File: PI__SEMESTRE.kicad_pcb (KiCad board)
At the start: 2 copper layers, 32 parts, among them IC1 LMV358IDR, J1 CX90B-16P1, U1 AMS1117, U11 ESP32-S3-WROOM-1, U14 BME688, U9 GUVA-S12SD

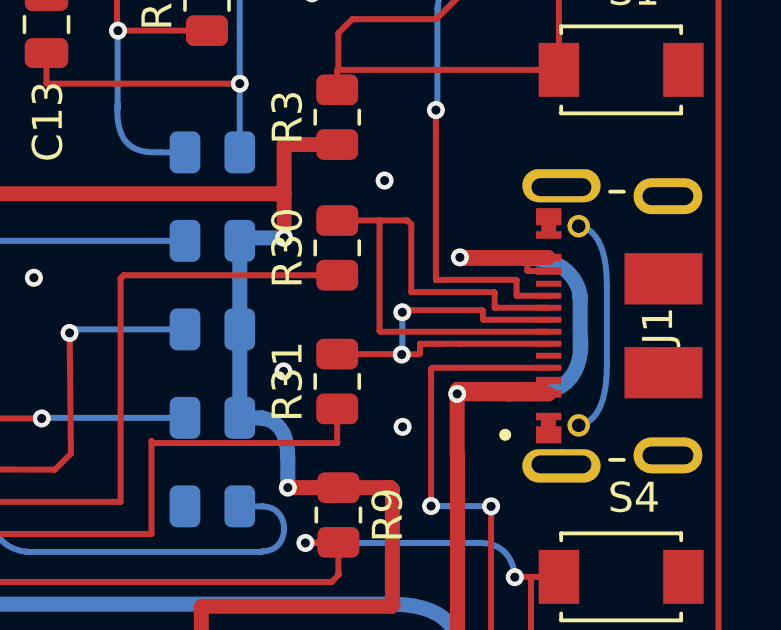
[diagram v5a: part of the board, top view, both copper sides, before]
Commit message: empece atrabajar las pistas rojas de la pcb
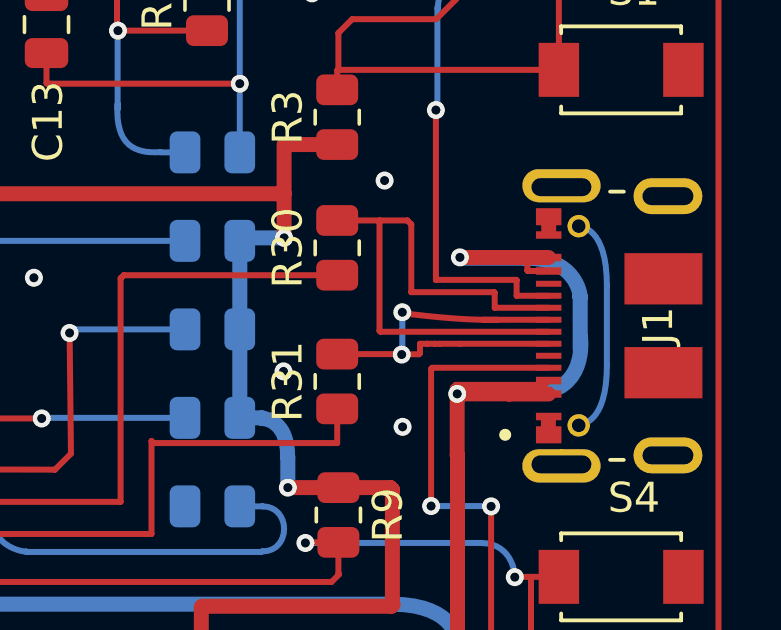
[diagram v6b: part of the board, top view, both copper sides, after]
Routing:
- net D+: track 14.1 -> 11.3 mm
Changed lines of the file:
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@@
 	(gr_curve
 		(pts
+			(xy 121.58 77.96) (xy 120.13 77.99) (xy 118.57 77.74) (xy 118.42 77.75)
+		)
+		(stroke
+			(width 0.2)
+			(type default)
+		)
+		(layer "F.Cu")
+		(net "D+")
+	)
+	(gr_curve
+		(pts
 			(xy 71.7 69.71) (xy 71.72 66.97) (xy 73.91 66.95) (xy 74.236277 66.935356)
 		)
@@
 	)
 	(segment
+		(start 83.05 72.98)
+		(end 83.05 75.82)
+		(width 0.2)
+		(layer "F.Cu")
+		(net "GPIO2")
+	)
+	(segment
+		(start 73.06 72.98)
+		(end 83.05 72.98)
+		(width 0.2)
+		(layer "F.Cu")
+		(net "GPIO2")
+	)
+	(segment
+		(start 72.96 72.88)
+		(end 73.06 72.98)
+		(width 0.2)
+		(layer "F.Cu")
+		(net "GPIO2")
+	)
+	(segment
+		(start 83.05 75.82)
+		(end 83.055 75.825)
+		(width 0.2)
+		(layer "F.Cu")
+		(net "GPIO2")
+	)
+	(segment
+		(start 83.055 75.825)
+		(end 83.14 75.91)
+		(width 0.2)
+		(layer "F.Cu")
+		(net "GPIO2")
+	)
+	(segment
+		(start 98.11 87.84)
+		(end 96.12 87.84)
+		(width 0.2)
+		(layer "F.Cu")
+		(net "GPIO2")
+	)
+	(segment
+		(start 98.11 89.07)
+		(end 98.11 87.84)
+		(width 0.2)
+		(layer "F.Cu")
+		(net "GPIO2")
+	)
+	(segment
+		(start 72.96 69.66)
+		(end 72.96 72.88)
+		(width 0.2)
+		(layer "F.Cu")
+		(net "GPIO2")
+	)
+	(via
+		(at 83.055 75.825)
+		(size 0.6)
+		(drill 0.3)
+		(layers "F.Cu" "B.Cu")
+		(net "GPIO2")
+	)
+	(via
+		(at 96.12 87.84)
+		(size 0.6)
+		(drill 0.3)
+		(layers "F.Cu" "B.Cu")
+		(net "GPIO2")
+	)
+	(segment
+		(start 83.055 75.825)
+		(end 83.01 75.87)
+		(width 0.2)
+		(layer "B.Cu")
+		(net "GPIO2")
+	)
+	(segment
+		(start 84.58 94.82)
+		(end 94.85 94.82)
+		(width 0.2)
+		(layer "B.Cu")
+		(net "GPIO2")
+	)
+	(segment
+		(start 83.01 75.87)
+		(end 83.01 93.25)
+		(width 0.2)
+		(layer "B.Cu")
+		(net "GPIO2")
+	)
+	(segment
+		(start 96.08 87.88)
+		(end 96.12 87.84)
+		(width 0.2)
+		(layer "B.Cu")
+		(net "GPIO2")
+	)
+	(segment
+		(start 96.08 93.53)
+		(end 96.08 87.88)
+		(width 0.2)
+		(layer "B.Cu")
+		(net "GPIO2")
+	)
+	(segment
 		(start 115.2 85.38)
 		(end 116.28 85.38)
@@
 	)
 	(segment
-		(start 118.686029 77.64)
-		(end 121.07 77.64)
-		(width 0.2)
-		(layer "F.Cu")
-		(net "D+")
-	)
-	(segment
-		(start 121.1 77.67)
-		(end 121.1 77.94)
-		(width 0.2)
-		(layer "F.Cu")
-		(net "D+")
-	)
-	(segment
 		(start 119 79.08)
 		(end 118.97 79.11)
@@
 	)
 	(segment
-		(start 121.07 77.64)
-		(end 121.1 77.67)
-		(width 0.2)
-		(layer "F.Cu")
-		(net "D+")
-	)
-	(segment
 		(start 119.504719 78.76)
 		(end 119.662915 78.76)
@@
 	)
 	(segment
-		(start 121.1 77.94)
-		(end 121.12 77.96)
-		(width 0.2)
-		(layer "F.Cu")
-		(net "D+")
-	)
-	(segment
 		(start 118.4 79.11)
 		(end 118.39 79.12)
@@
 	)
 	(segment
-		(start 118.616029 77.71)
-		(end 118.686029 77.64)
-		(width 0.2)
-		(layer "F.Cu")
-		(net "D+")
-	)
-	(segment
 		(start 118.41 77.71)
 		(end 118.616029 77.71)
@@
 		(net "Net-(J1-MID_PLATE-PadMID1)")
 	)
-	(segment
-		(start 83.05 72.98)
-		(end 83.05 75.82)
-		(width 0.2)
-		(layer "F.Cu")
-		(net "GPIO2")
-	)
-	(segment
-		(start 73.06 72.98)
-		(end 83.05 72.98)
-		(width 0.2)
-		(layer "F.Cu")
-		(net "GPIO2")
-	)
-	(segment
-		(start 72.96 72.88)
-		(end 73.06 72.98)
-		(width 0.2)
-		(layer "F.Cu")
-		(net "GPIO2")
-	)
-	(segment
-		(start 83.05 75.82)
-		(end 83.055 75.825)
-		(width 0.2)
-		(layer "F.Cu")
-		(net "GPIO2")
-	)
-	(segment
-		(start 83.055 75.825)
-		(end 83.14 75.91)
-		(width 0.2)
-		(layer "F.Cu")
-		(net "GPIO2")
-	)
-	(segment
-		(start 98.11 87.84)
-		(end 96.12 87.84)
-		(width 0.2)
-		(layer "F.Cu")
-		(net "GPIO2")
-	)
-	(segment
-		(start 98.11 89.07)
-		(end 98.11 87.84)
-		(width 0.2)
-		(layer "F.Cu")
-		(net "GPIO2")
-	)
-	(segment
-		(start 72.96 69.66)
-		(end 72.96 72.88)
-		(width 0.2)
-		(layer "F.Cu")
-		(net "GPIO2")
-	)
-	(via
-		(at 83.055 75.825)
-		(size 0.6)
-		(drill 0.3)
-		(layers "F.Cu" "B.Cu")
-		(net "GPIO2")
-	)
-	(via
-		(at 96.12 87.84)
-		(size 0.6)
-		(drill 0.3)
-		(layers "F.Cu" "B.Cu")
-		(net "GPIO2")
-	)
-	(segment
-		(start 83.055 75.825)
-		(end 83.01 75.87)
-		(width 0.2)
-		(layer "B.Cu")
-		(net "GPIO2")
-	)
-	(segment
-		(start 84.58 94.82)
-		(end 94.85 94.82)
-		(width 0.2)
-		(layer "B.Cu")
-		(net "GPIO2")
-	)
-	(segment
-		(start 83.01 75.87)
-		(end 83.01 93.25)
-		(width 0.2)
-		(layer "B.Cu")
-		(net "GPIO2")
-	)
-	(segment
-		(start 96.08 87.88)
-		(end 96.12 87.84)
-		(width 0.2)
-		(layer "B.Cu")
-		(net "GPIO2")
-	)
-	(segment
-		(start 96.08 93.53)
-		(end 96.08 87.88)
-		(width 0.2)
-		(layer "B.Cu")
-		(net "GPIO2")
-	)
 	(zone

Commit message: ignorar
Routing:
- net D-: track 19.2 -> 17.4 mm
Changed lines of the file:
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@@
+	(gr_curve
+		(pts
+			(xy 117.66 77.79) (xy 117.66 77.79) (xy 117.66 77.79) (xy 117.66 77.79)
+		)
+		(stroke
+			(width 0.2)
+			(type default)
+		)
+		(layer "F.Cu")
+	)
+	(gr_curve
+		(pts
+			(xy 117.78 78.16) (xy 117.78 78.16) (xy 117.78 78.16) (xy 117.78 78.16)
+		)
+		(stroke
+			(width 0.2)
+			(type default)
+		)
+		(layer "F.Cu")
+	)
+	(gr_curve
+		(pts
+			(xy 117.95 78.16) (xy 117.95 78.16) (xy 117.95 78.16) (xy 117.95 78.16)
+		)
+		(stroke
+			(width 0.2)
+			(type default)
+		)
+		(layer "F.Cu")
+	)
+	(gr_curve
+		(pts
+			(xy 118.132243 78.36) (xy 118.13 78.36) (xy 117.63 78.41) (xy 117.65 77.78)
+		)
+		(stroke
+			(width 0.2)
+			(type default)
+		)
+		(layer "F.Cu")
+		(net "D-")
+	)
+	(gr_curve
+		(pts
+			(xy 119.28 77.04) (xy 119.1 77.06) (xy 118.69 77.04) (xy 118.711185 76.600764)
+		)
+		(stroke
+			(width 0.2)
+			(type default)
+		)
+		(layer "F.Cu")
+		(net "D-")
+	)
 	(gr_curve
 		(pts
@@
 	)
 	(segment
-		(start 121.49 77.56)
-		(end 123.29 77.56)
+		(start 118.71 76.64)
+		(end 118.71 74.78)
+		(width 0.2)
+		(layer "F.Cu")
+		(net "D-")
+	)
+	(segment
+		(start 121.49 77.06)
+		(end 121.47 77.04)
+		(width 0.2)
+		(layer "F.Cu")
+		(net "D-")
+	)
+	(segment
+		(start 123.29 78.36)
+		(end 118.11 78.36)
+		(width 0.2)
+		(layer "F.Cu")
+		(net "D-")
+	)
+	(segment
+		(start 118.58 74.65)
+		(end 117.66 74.65)
+		(width 0.2)
+		(layer "F.Cu")
+		(net "D-")
+	)
+	(segment
+		(start 117.65 74.66)
+		(end 117.66 74.65)
+		(width 0.2)
+		(layer "F.Cu")
+		(net "D-")
+	)
+	(segment
+		(start 123.29 77.56)
+		(end 121.581281 77.56)
+		(width 0.2)
+		(layer "F.Cu")
+		(net "D-")
+	)
+	(segment
+		(start 121.49 77.559449)
+		(end 121.49 77.06)
+		(width 0.2)
+		(layer "F.Cu")
+		(net "D-")
+	)
+	(segment
+		(start 121.581281 77.56)
+		(end 121.49 77.559449)
+		(width 0.2)
+		(layer "F.Cu")
+		(net "D-")
+	)
+	(segment
+		(start 117.65 77.79)
+		(end 117.65 74.66)
+		(width 0.2)
+		(layer "F.Cu")
+		(net "D-")
+	)
+	(segment
+		(start 121.47 77.04)
+		(end 119.11 77.04)
+		(width 0.2)
+		(layer "F.Cu")
+		(net "D-")
+	)
+	(segment
+		(start 117.66 74.65)
+		(end 116.24 74.65)
 		(width 0.2)
 		(layer "F.Cu")
@@
 		(width 0.2)
 		(layer "F.Cu")
-		(net "D-")
-	)
-	(segment
-		(start 118.71 77.04)
-		(end 118.71 74.78)
-		(width 0.2)
-		(layer "F.Cu")
-		(net "D-")
-	)
-	(segment
-		(start 117.65 78.33)
-		(end 117.65 74.66)
-		(width 0.2)
-		(layer "F.Cu")
-		(net "D-")
-	)
-	(segment
-		(start 117.68 78.36)
-		(end 117.65 78.33)
-		(width 0.2)
-		(layer "F.Cu")
-		(net "D-")
-	)
-	(segment
-		(start 117.65 74.66)
-		(end 117.66 74.65)
-		(width 0.2)
-		(layer "F.Cu")
-		(net "D-")
-	)
-	(segment
-		(start 118.58 74.65)
-		(end 117.66 74.65)
-		(width 0.2)
-		(layer "F.Cu")
-		(net "D-")
-	)
-	(segment
-		(start 123.29 78.36)
-		(end 117.68 78.36)
-		(width 0.2)
-		(layer "F.Cu")
-		(net "D-")
-	)
-	(segment
-		(start 118.71 77.04)
-		(end 121.47 77.04)
-		(width 0.2)
-		(layer "F.Cu")
-		(net "D-")
-	)
-	(segment
-		(start 121.47 77.04)
-		(end 121.49 77.06)
-		(width 0.2)
-		(layer "F.Cu")
-		(net "D-")
-	)
-	(segment
-		(start 117.66 74.65)
-		(end 116.24 74.65)
-		(width 0.2)
-		(layer "F.Cu")
-		(net "D-")
-	)
-	(segment
-		(start 121.49 77.06)
-		(end 121.49 77.56)
-		(width 0.2)
-		(layer "F.Cu")

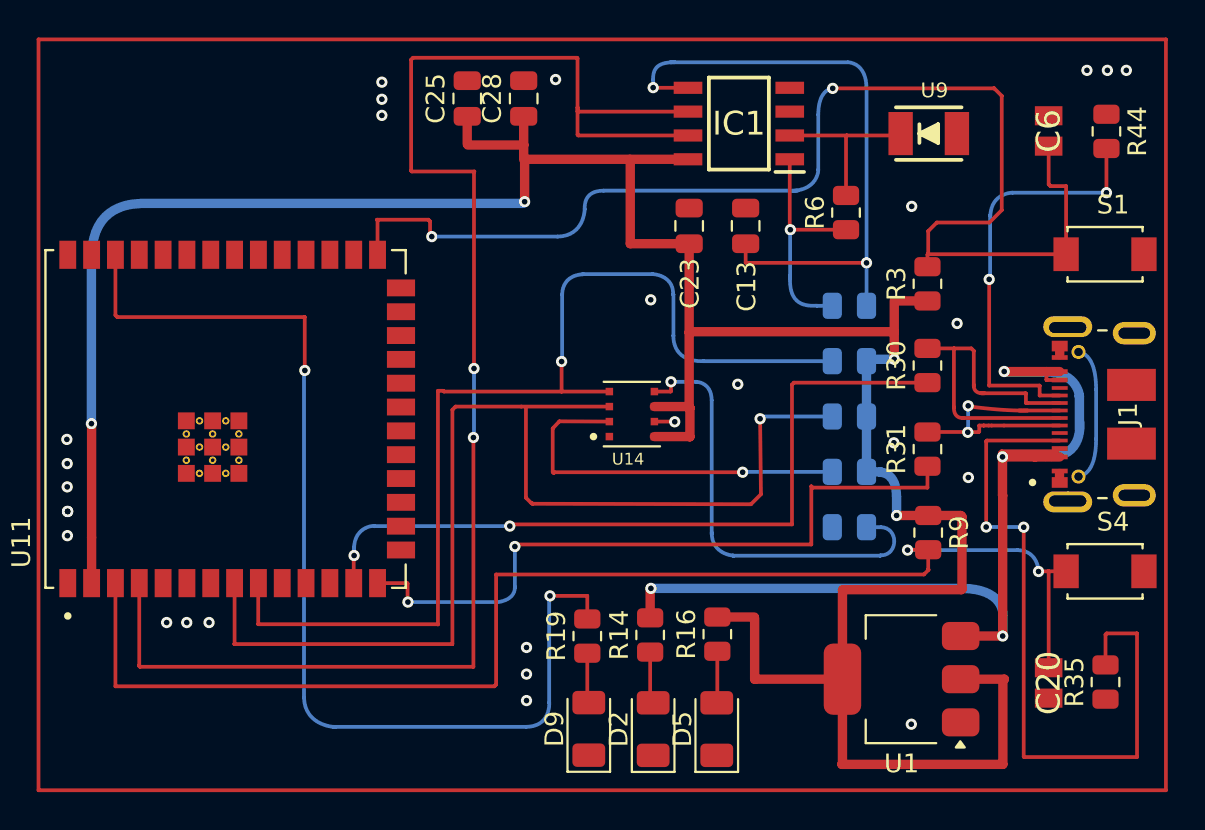
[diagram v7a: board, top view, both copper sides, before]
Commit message: Se corrigió el tamaño de algunas pistas y también se ajustaron las curvas en las esquinas, con el fin de evitar terminaciones en punta. De esta manera, las pistas quedan con un trazado más limpio, uniforme y adecuado para el diseño de la PCB.
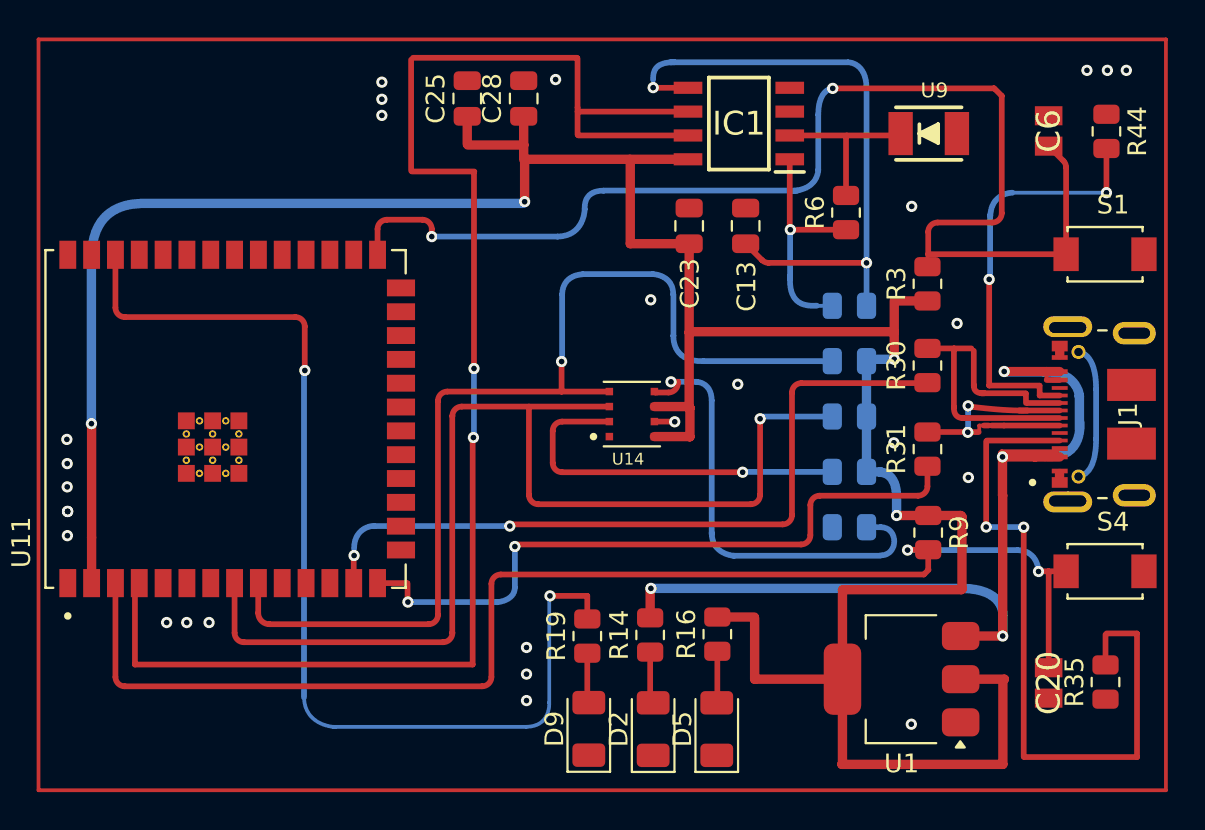
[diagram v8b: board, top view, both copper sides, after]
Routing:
- net ADC ESP32: track 83.1 -> 48.6 mm
- net I2C_SCL: track 51.4 -> 50.6 mm
- net I2C_SDA: track 61.3 -> 60.5 mm
- net Net-(U11-USB_D+): track 35.8 -> 35.0 mm
- net EN: track 69.5 -> 68.9 mm
- net Filtro: track 30.7 -> 30.1 mm
- net Boot: track 61.2 -> 60.6 mm
- net Net-(U14-SDO): track 18.5 -> 19.1 mm
